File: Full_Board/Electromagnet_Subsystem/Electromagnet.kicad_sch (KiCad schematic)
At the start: 0 parts

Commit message: Added electromagnet circuit and adjusted the bypass caps
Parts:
- added C31: 0.1 uF, CL10B104KB8NNNC:CL10B104KB8NNNC, symbol Device:C
- added C32: 470 uF, EEE-FP1E471AP:EEE-FP1E471AP, symbol Device:C_Polarized_US
- added IC7: DRV8210DRLR, DRV8210DRLR:SOTFL50P160X60-6N, symbol DRV8210DRLR:DRV8210DRLR
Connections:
- new net 5v: C31.1, C32.1, IC7.5 (VM)
- new net GND: C31.2, C32.2, IC7.3 (GND)
- new net IN1: IC7.2 (IN2)
- new net IN2: IC7.1 (IN1)
- new net OUT1: IC7.6 (OUT1)
- new net OUT2: IC7.4 (OUT2)
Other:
- note added: "Electromagnet Driver"
- note added: "Notes C31 is a bypass capacitor C32 is a bulk capacitor This particular chip only supports PWM control through the IN1 and IN2 pins This is configured in as a full bridge"
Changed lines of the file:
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@@
     (company "The Great Gambit")
   )
+  (junction (at 170.18 87.63) (diameter 0) (color 0 0 0 0)
+  )
+  (junction (at 177.8 87.63) (diameter 0) (color 0 0 0 0)
+  )
+  (junction (at 173.99 101.6) (diameter 0) (color 0 0 0 0)
+  )
+  (wire (pts (xy 177.8 87.63) (xy 177.8 90.17))
+    (stroke (width 0) (type default) (color 0 0 0 0))
+  )
+  (polyline (pts (xy 106.68 69.85) (xy 106.68 71.12))
+    (stroke (width 0) (type default) (color 0 0 0 0))
+  )
+  (polyline (pts (xy 106.68 71.12) (xy 106.68 113.03))
+    (stroke (width 0) (type default) (color 0 0 0 0))
+  )
+  (wire (pts (xy 119.38 87.63) (xy 123.19 87.63))
+    (stroke (width 0) (type default) (color 0 0 0 0))
+  )
+  (wire (pts (xy 151.13 90.17) (xy 153.67 90.17))
+    (stroke (width 0) (type default) (color 0 0 0 0))
+  )
+  (polyline (pts (xy 106.68 113.03) (xy 190.5 113.03))
+    (stroke (width 0) (type default) (color 0 0 0 0))
+  )
+  (wire (pts (xy 177.8 87.63) (xy 181.61 87.63))
+    (stroke (width 0) (type default) (color 0 0 0 0))
+  )
+  (wire (pts (xy 119.38 90.17) (xy 123.19 90.17))
+    (stroke (width 0) (type default) (color 0 0 0 0))
+  )
+  (wire (pts (xy 170.18 101.6) (xy 173.99 101.6))
+    (stroke (width 0) (type default) (color 0 0 0 0))
+  )
+  (wire (pts (xy 119.38 85.09) (xy 123.19 85.09))
+    (stroke (width 0) (type default) (color 0 0 0 0))
+  )
+  (wire (pts (xy 170.18 87.63) (xy 170.18 90.17))
+    (stroke (width 0) (type default) (color 0 0 0 0))
+  )
+  (wire (pts (xy 177.8 101.6) (xy 173.99 101.6))
+    (stroke (width 0) (type default) (color 0 0 0 0))
+  )
+  (wire (pts (xy 170.18 97.79) (xy 170.18 101.6))
+    (stroke (width 0) (type default) (color 0 0 0 0))
+  )
+  (wire (pts (xy 151.13 85.09) (xy 153.67 85.09))
+    (stroke (width 0) (type default) (color 0 0 0 0))
+  )
+  (wire (pts (xy 173.99 101.6) (xy 173.99 102.87))
+    (stroke (width 0) (type default) (color 0 0 0 0))
+  )
+  (wire (pts (xy 151.13 87.63) (xy 170.18 87.63))
+    (stroke (width 0) (type default) (color 0 0 0 0))
+  )
+  (polyline (pts (xy 190.5 69.85) (xy 106.68 69.85))
+    (stroke (width 0) (type default) (color 0 0 0 0))
+  )
+  (wire (pts (xy 177.8 97.79) (xy 177.8 101.6))
+    (stroke (width 0) (type default) (color 0 0 0 0))
+  )
+  (polyline (pts (xy 190.5 113.03) (xy 190.5 69.85))
+    (stroke (width 0) (type default) (color 0 0 0 0))
+  )
+  (wire (pts (xy 170.18 87.63) (xy 177.8 87.63))
+    (stroke (width 0) (type default) (color 0 0 0 0))
+  )
+  (text "Notes\n	C31 is a bypass capacitor\n	C32 is a bulk capacitor\n	This particular chip only supports PWM control through the IN1 and IN2 pins\n	This is configured in as a full bridge"
+    (at 16.51 25.4 0)
+    (effects (font (size 1.27 1.27)) (justify left bottom))
+  )
+  (text "Electromagnet Driver" (at 168.91 111.76 0)
+    (effects (font (size 1.27 1.27) (thickness 0.254) bold) (justify left bottom))
+  )
+  (hierarchical_label "OUT2" (shape output) (at 153.67 85.09 0)
+    (effects (font (size 1.27 1.27)) (justify left))
+  )
+  (hierarchical_label "OUT1" (shape output) (at 153.67 90.17 0)
+    (effects (font (size 1.27 1.27)) (justify left))
+  )
+  (hierarchical_label "GND" (shape input) (at 173.99 102.87 270)
+    (effects (font (size 1.27 1.27)) (justify right))
+  )
+  (hierarchical_label "5v" (shape input) (at 181.61 87.63 0)
+    (effects (font (size 1.27 1.27)) (justify left))
+  )
+  (hierarchical_label "IN2" (shape input) (at 119.38 85.09 180)
+    (effects (font (size 1.27 1.27)) (justify right))
+  )
+  (hierarchical_label "GND" (shape input) (at 119.38 90.17 180)
+    (effects (font (size 1.27 1.27)) (justify right))
+  )
+  (hierarchical_label "IN1" (shape input) (at 119.38 87.63 180)
+    (effects (font (size 1.27 1.27)) (justify right))
+  )
+  (symbol (lib_id "Device:C_Polarized_US") (at 177.8 93.98 0) (unit 1)
+    (in_bom yes) (on_board yes) (fields_autoplaced)
+    (property "Reference" "C32" (id 0) (at 181.61 92.0749 0)
+      (effects (font (size 1.27 1.27)) (justify left))
+    )
+    (property "Value" "470 uF" (id 1) (at 181.61 94.6149 0)
+      (effects (font (size 1.27 1.27)) (justify left))
+    )
+    (property "Footprint" "EEE-FP1E471AP:EEE-FP1E471AP" (id 2) (at 177.8 93.98 0)
+      (effects (font (size 1.27 1.27)) hide)
+    )
+    (property "Datasheet" "~" (id 3) (at 177.8 93.98 0)
+      (effects (font (size 1.27 1.27)) hide)
+    )
+    (property "Manufacturers Part Number" "EEE-FP1E471AP" (id 4) (at 177.8 93.98 0)
+      (effects (font (size 1.27 1.27)) hide)
+    )
+    (property "Digikey Part Number" "PCE4440DKR-ND" (id 5) (at 177.8 93.98 0)
+      (effects (font (size 1.27 1.27)) hide)
+    )
+    (property "Mouser Part Number" "" (id 6) (at 177.8 93.98 0)
+      (effects (font (size 1.27 1.27)) hide)
+    )
+    (property "Digikey Link" "https://www.digikey.com/en/products/detail/panasonic-electronic-components/EEE-FP1E471AP/1245939" (id 7) (at 177.8 93.98 0)
+      (effects (font (size 1.27 1.27)) hide)
+    )
+    (property "Mouser Link" "" (id 8) (at 177.8 93.98 0)
+      (effects (font (size 1.27 1.27)) hide)
+    )
+    (pin "1")
+    (pin "2")
+  )
+  (symbol (lib_id "DRV8210DRLR:DRV8210DRLR") (at 123.19 85.09 0) (unit 1)
+    (in_bom yes) (on_board yes) (fields_autoplaced)
+    (property "Reference" "IC7" (id 0) (at 137.16 77.47 0))
+    (property "Value" "DRV8210DRLR" (id 1) (at 137.16 80.01 0))
+    (property "Footprint" "DRV8210DRLR:SOTFL50P160X60-6N" (id 2) (at 147.32 82.55 0)
+      (effects (font (size 1.27 1.27)) (justify left) hide)
+    )
+    (property "Datasheet" "https://www.ti.com/lit/ds/symlink/drv8210.pdf?ts=1641207817417&ref_url=https%253A%252F%252Fwww.google.com%252F" (id 3) (at 147.32 85.09 0)
+      (effects (font (size 1.27 1.27)) (justify left) hide)
+    )
+    (property "Manufacturer Part Number" "DRV8210DRLR" (id 9) (at 147.32 100.33 0)
+      (effects (font (size 1.27 1.27)) (justify left) hide)
+    )
+    (property "Digikey Part Number" "296-DRV8210DRLRDKR-ND" (id 10) (at 123.19 85.09 0)
+      (effects (font (size 1.27 1.27)) hide)
+    )
+    (property "Mouser Part Number" "595-DRV8210DRLR" (id 6) (at 147.32 92.71 0)
+      (effects (font (size 1.27 1.27)) (justify left) hide)
+    )
+    (property "Digikey Link" "https://www.digikey.com/en/products/detail/texas-instruments/DRV8210DRLR/15286847" (id 11) (at 123.19 85.09 0)
+      (effects (font (size 1.27 1.27)) hide)
+    )
+    (property "Mouser Link" "https://www.mouser.com/ProductDetail/Texas-Instruments/DRV8210DRLR?qs=7D1LtPJG0i1B1CHsXZuruQ%3D%3D" (id 12) (at 123.19 85.09 0)
+      (effects (font (size 1.27 1.27)) hide)
+    )
+    (property "Description" "Motor / Motion / Ignition Controllers & Drivers 12-V, 1.76-A brushed DC motor driver with auto sleep mode" (id 4) (at 147.32 87.63 0)
+      (effects (font (size 1.27 1.27)) (justify left) hide)
+    )
+    (property "Height" "0.6" (id 5) (at 147.32 90.17 0)
+      (effects (font (size 1.27 1.27)) (justify left) hide)
+    )
+    (property "Mouser Price/Stock" "https://www.mouser.co.uk/ProductDetail/Texas-Instruments/DRV8210DRLR?qs=7D1LtPJG0i1B1CHsXZuruQ%3D%3D" (id 7) (at 147.32 95.25 0)
+      (effects (font (size 1.27 1.27)) (justify left) hide)
+    )
+    (property "Manufacturer_Name" "Texas Instruments" (id 8) (at 147.32 97.79 0)
+      (effects (font (size 1.27 1.27)) (justify left) hide)
+    )
+    (pin "1")
+    (pin "2")
+    (pin "3")
+    (pin "4")
+    (pin "5")
+    (pin "6")
+  )
+  (symbol (lib_id "Device:C") (at 170.18 93.98 0) (unit 1)
+    (in_bom yes) (on_board yes)
+    (property "Reference" "C31" (id 0) (at 162.56 93.98 0)
+      (effects (font (size 1.27 1.27)) (justify left))
+    )
+    (property "Value" "0.1 uF" (id 1) (at 162.56 96.52 0)
+      (effects (font (size 1.27 1.27)) (justify left))
+    )
+    (property "Footprint" "CL10B104KB8NNNC:CL10B104KB8NNNC" (id 2) (at 171.1452 97.79 0)
+      (effects (font (size 1.27 1.27)) hide)
+    )
+    (property "Datasheet" "https://media.digikey.com/pdf/Data%20Sheets/Samsung%20PDFs/CL10B104KB8NNNC_Spec.pdf" (id 3) (at 170.18 93.98 0)
+      (effects (font (size 1.27 1.27)) hide)
+    )
+    (property "Manufacturers Part Number" "CL10B104KB8NNNC" (id 4) (at 170.18 93.98 0)
+      (effects (font (size 1.27 1.27)) hide)
+    )
+    (property "Digikey Part Number" "1276-1000-6-ND" (id 5) (at 170.18 93.98 0)
+      (effects (font (size 1.27 1.27)) hide)
+    )
+    (property "Mouser Part Number" "" (id 6) (at 170.18 93.98 0)
+      (effects (font (size 1.27 1.27)) hide)
+    )
+    (property "Digikey Link" "https://www.digikey.com/en/products/detail/samsung-electro-mechanics/CL10B104KB8NNNC/3886658" (id 7) (at 170.18 93.98 0)
+      (effects (font (size 1.27 1.27)) hide)
+    )
+    (property "Mouser Link" "" (id 8) (at 170.18 93.98 0)
+      (effects (font (size 1.27 1.27)) hide)
+    )
+    (pin "1")
+    (pin "2")
+  )
 )

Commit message: Resolve misconfigured components, replace PCB from now completed schematic
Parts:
- IC7: footprint DRV8210DRLR:SOTFL50P160X60-6N -> SOTFL50P160X60-6N; Manufacturer_Part_Number (none) -> DRV8210DRLR
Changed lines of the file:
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@@
     (property "Reference" "IC7" (id 0) (at 137.16 77.47 0))
     (property "Value" "DRV8210DRLR" (id 1) (at 137.16 80.01 0))
-    (property "Footprint" "DRV8210DRLR:SOTFL50P160X60-6N" (id 2) (at 147.32 82.55 0)
+    (property "Footprint" "SOTFL50P160X60-6N" (id 2) (at 147.32 82.55 0)
       (effects (font (size 1.27 1.27)) (justify left) hide)
     )
@@
       (effects (font (size 1.27 1.27)) (justify left) hide)
     )
+    (property "Manufacturer_Part_Number" "DRV8210DRLR" (id 13) (at 147.32 100.33 0)
+      (effects (font (size 1.27 1.27)) (justify left) hide)
+    )
     (pin "1")
     (pin "2")
@@
       (effects (font (size 1.27 1.27)) hide)
     )
-    (property "Datasheet" "https://media.digikey.com/pdf/Data%20Sheets/Samsung%20PDFs/CL10B104KB8NNNC_Spec.pdf" (id 3) (at 170.18 93.98 0)
+    (property "Datasheet" "~" (id 3) (at 170.18 93.98 0)
       (effects (font (size 1.27 1.27)) hide)
     )

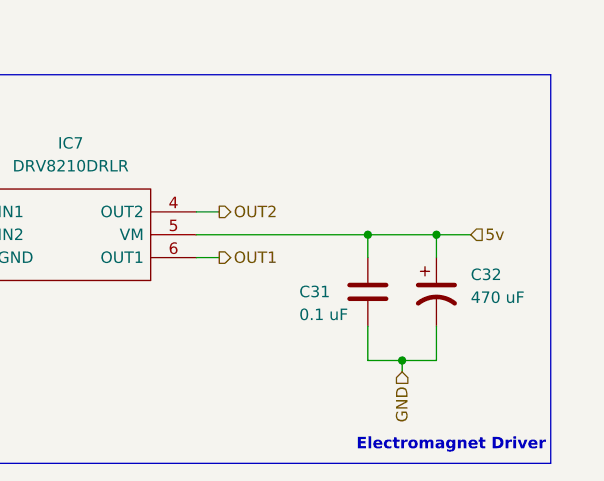
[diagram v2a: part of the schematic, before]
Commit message: Redo pinout, finish pcb layout (no traces)
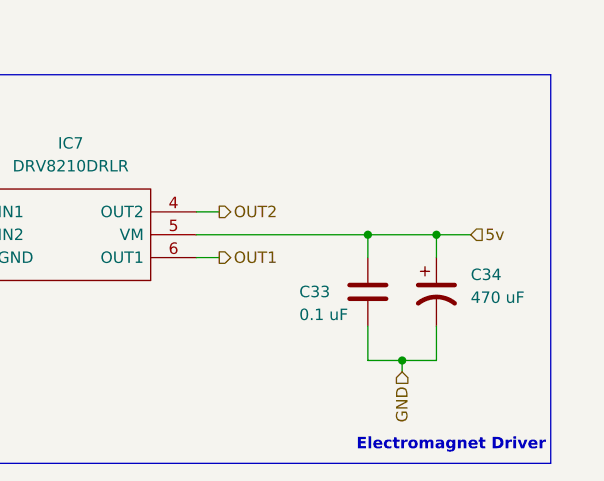
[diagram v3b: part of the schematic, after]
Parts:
- renumbered C31 to C33, C32 to C34
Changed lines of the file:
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@@
   (symbol (lib_id "Device:C_Polarized_US") (at 177.8 93.98 0) (unit 1)
     (in_bom yes) (on_board yes) (fields_autoplaced)
-    (property "Reference" "C32" (id 0) (at 181.61 92.0749 0)
+    (property "Reference" "C34" (id 0) (at 181.61 92.0749 0)
       (effects (font (size 1.27 1.27)) (justify left))
     )
@@
   (symbol (lib_id "Device:C") (at 170.18 93.98 0) (unit 1)
     (in_bom yes) (on_board yes)
-    (property "Reference" "C31" (id 0) (at 162.56 93.98 0)
+    (property "Reference" "C33" (id 0) (at 162.56 93.98 0)
       (effects (font (size 1.27 1.27)) (justify left))
     )

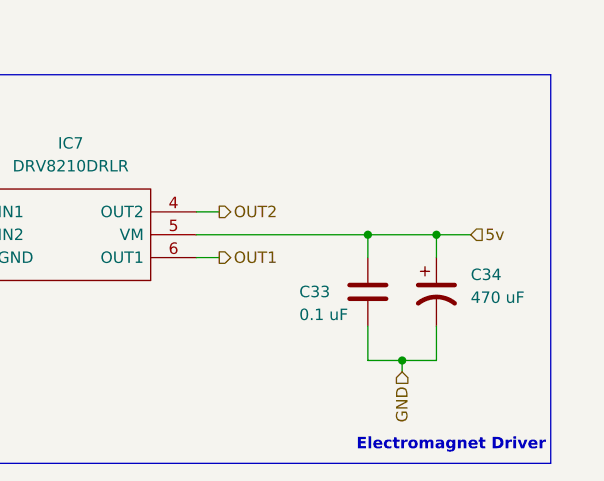
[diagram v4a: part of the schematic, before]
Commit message: Fix vias for Analog Digital's requirements
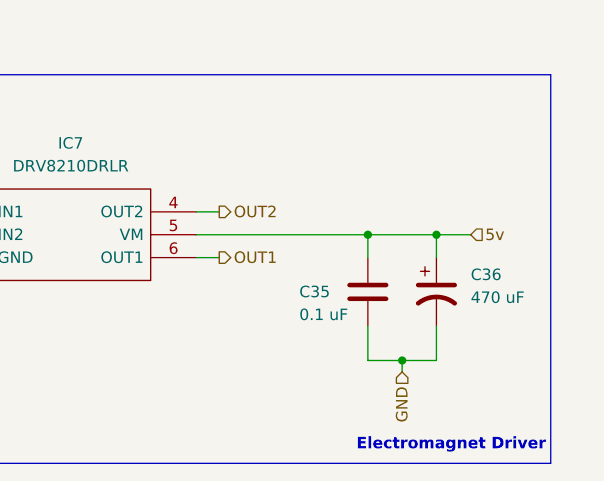
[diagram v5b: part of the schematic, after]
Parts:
- renumbered C33 to C35, C34 to C36
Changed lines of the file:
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@@
   (symbol (lib_id "Device:C_Polarized_US") (at 177.8 93.98 0) (unit 1)
     (in_bom yes) (on_board yes) (fields_autoplaced)
-    (property "Reference" "C34" (id 0) (at 181.61 92.0749 0)
+    (property "Reference" "C36" (id 0) (at 181.61 92.0749 0)
       (effects (font (size 1.27 1.27)) (justify left))
     )
@@
   (symbol (lib_id "Device:C") (at 170.18 93.98 0) (unit 1)
     (in_bom yes) (on_board yes)
-    (property "Reference" "C33" (id 0) (at 162.56 93.98 0)
+    (property "Reference" "C35" (id 0) (at 162.56 93.98 0)
       (effects (font (size 1.27 1.27)) (justify left))
     )

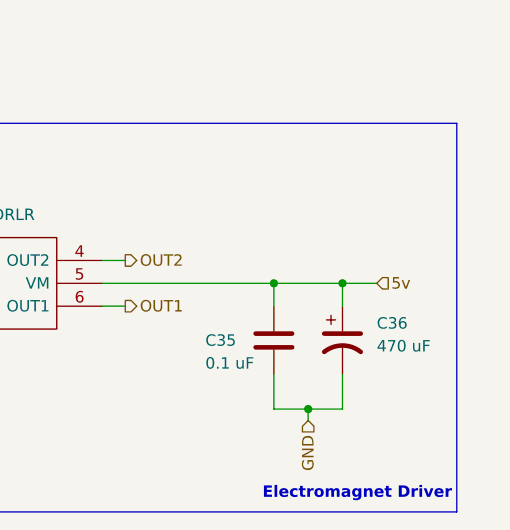
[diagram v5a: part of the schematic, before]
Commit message: Swapped resistors in stepper driver
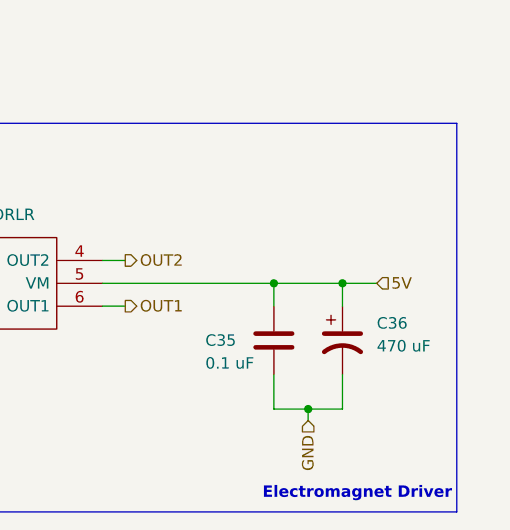
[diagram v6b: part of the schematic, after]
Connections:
- net 5v renamed 5V
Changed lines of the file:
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@@
     (effects (font (size 1.27 1.27)) (justify right))
   )
-  (hierarchical_label "5v" (shape input) (at 181.61 87.63 0)
+  (hierarchical_label "5V" (shape input) (at 181.61 87.63 0)
     (effects (font (size 1.27 1.27)) (justify left))
   )

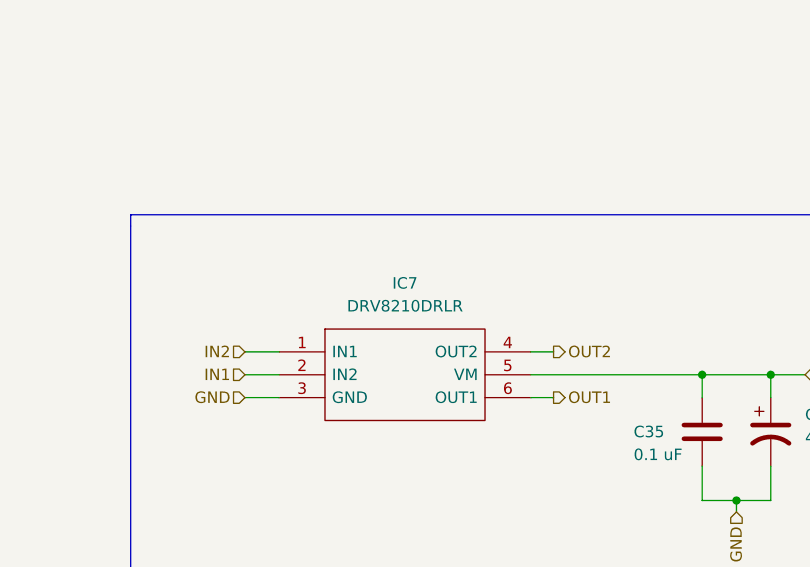
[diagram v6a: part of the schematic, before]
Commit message: Replace MUX/DEMUX; DRC passes aside from electromagnet
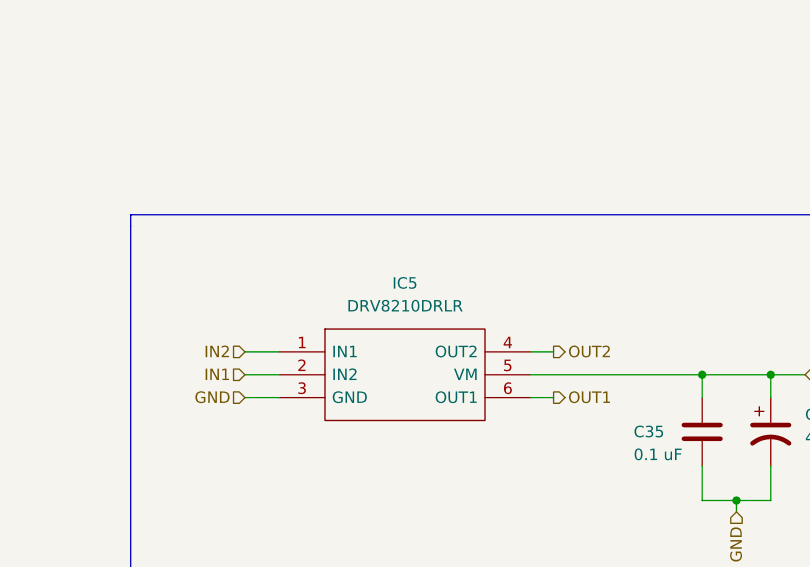
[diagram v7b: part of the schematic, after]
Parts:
- renumbered IC7 to IC5
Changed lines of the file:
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@@
   (symbol (lib_id "DRV8210DRLR:DRV8210DRLR") (at 123.19 85.09 0) (unit 1)
     (in_bom yes) (on_board yes) (fields_autoplaced)
-    (property "Reference" "IC7" (id 0) (at 137.16 77.47 0))
+    (property "Reference" "IC5" (id 0) (at 137.16 77.47 0))
     (property "Value" "DRV8210DRLR" (id 1) (at 137.16 80.01 0))
     (property "Footprint" "SOTFL50P160X60-6N" (id 2) (at 147.32 82.55 0)
